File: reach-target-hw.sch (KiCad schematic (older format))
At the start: 53 parts, among them J101 CONN_01X02, J102 CONN_01X02, J103 CONN_02X05, J104 MODULE_HEADER, J105 MODULE_HEADER, J106 MODULE_HEADER, P101 CONN_01X05, P102 CONN_01X05, P103 CONN_01X02, P104 CONN_01X02, P105 CONN_01X05, P106 CONN_01X05, SW101 SW_PUSH, U1 nRF51822-QF, U101 CAT24C02YI-GT3A, U102 NCP103AMX330, X1 CX2520DB16000D0GEJCC, X2 SC32S-12.5PF20PPM

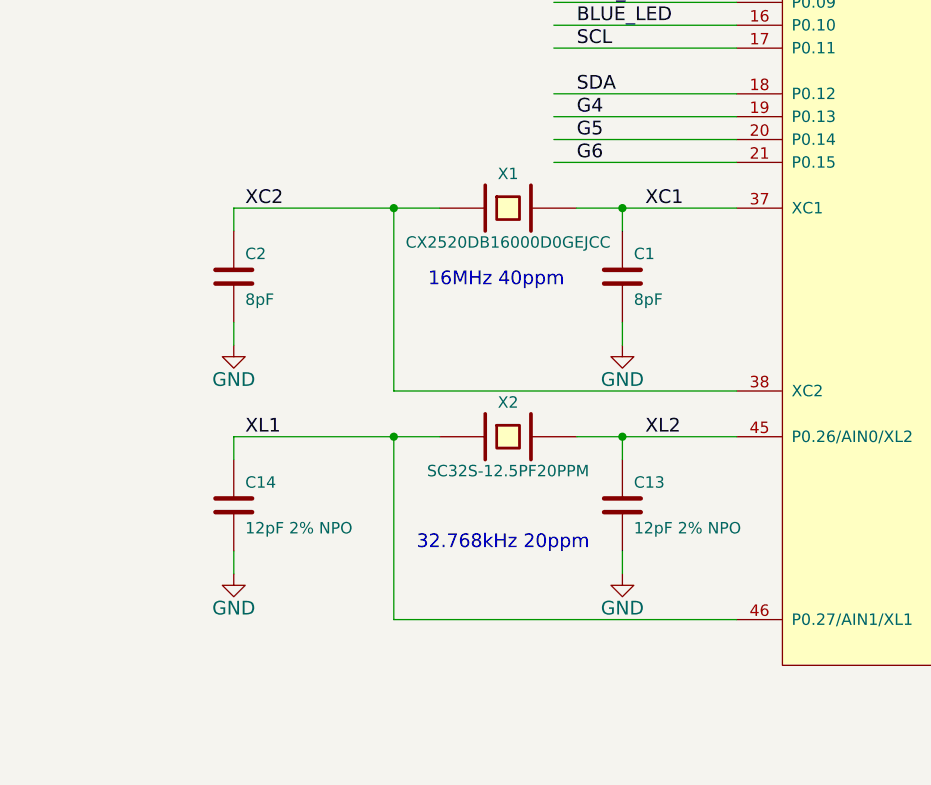
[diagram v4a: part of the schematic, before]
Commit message: ignore the last message... tweaked battery monitor, found real crystals
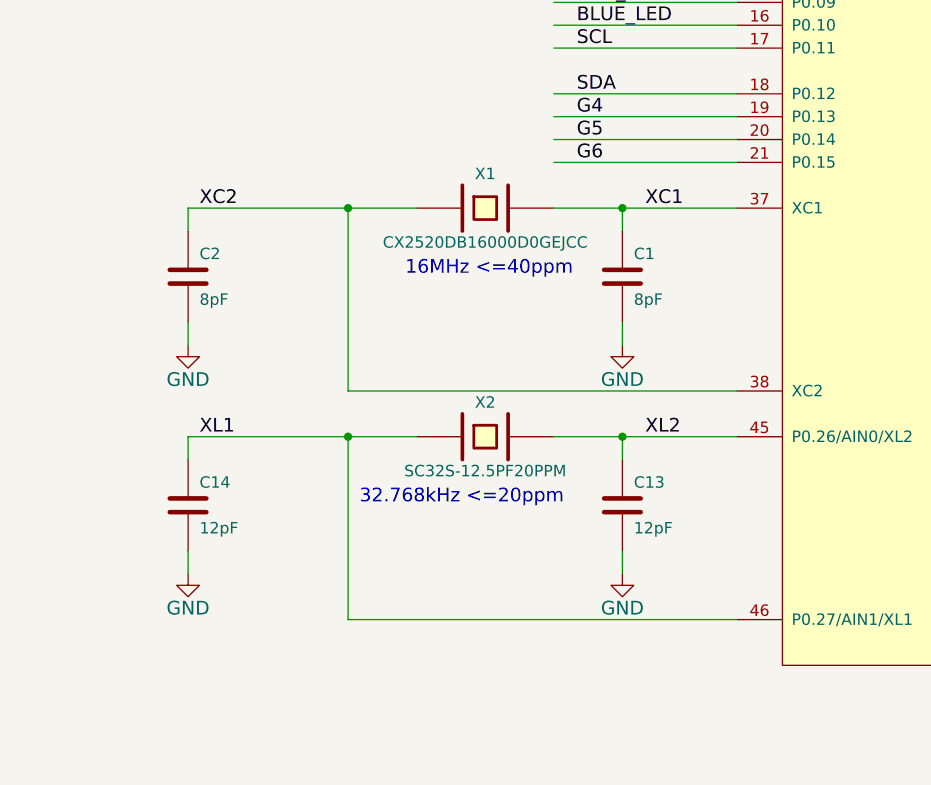
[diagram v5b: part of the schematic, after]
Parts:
- C13, C14: value 12pF 2% NPO -> 12pF
- X1: footprint (none) -> !Parts:CX2520DB
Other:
- note added: "16MHz <=40ppm"
- note added: "32.768kHz <=20ppm"
- note removed: "16MHz 40ppm"
- note removed: "32.768kHz 20ppm"
- moved on the sheet: C14, C2, X1, X2
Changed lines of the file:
@@
 L CRYSTAL X1
 U 1 1 54D12781
-P 6500 5200
-F 0 "X1" H 6500 5350 50  0000 C CNN
-F 1 "CX2520DB16000D0GEJCC" H 6500 5050 50  0000 C CNN
-F 2 "" H 6500 5200 60  0001 C CNN
-F 3 "" H 6500 5200 60  0000 C CNN
-	1    6500 5200
+P 6400 5200
+F 0 "X1" H 6400 5350 50  0000 C CNN
+F 1 "CX2520DB16000D0GEJCC" H 6400 5050 50  0000 C CNN
+F 2 "!Parts:CX2520DB" H 6400 5200 60  0001 C CNN
+F 3 "http://www.kyocera-crystal.jp/eng/wp-content/uploads/2014/09/cx2520db_e.pdf" H 6400 5200 60  0001 C CNN
+	1    6400 5200
 	1    0    0    -1
 $EndComp
@@
 L C C2
 U 1 1 54D14813
-P 5300 5500
-F 0 "C2" H 5350 5600 50  0000 L CNN
-F 1 "8pF" H 5350 5400 50  0000 L CNN
-F 2 "!Parts:SMD-0402" H 5338 5350 30  0001 C CNN
-F 3 "" H 5300 5500 60  0000 C CNN
-	1    5300 5500
+P 5100 5500
+F 0 "C2" H 5150 5600 50  0000 L CNN
+F 1 "8pF" H 5150 5400 50  0000 L CNN
+F 2 "!Parts:SMD-0402" H 5138 5350 30  0001 C CNN
+F 3 "" H 5100 5500 60  0000 C CNN
+	1    5100 5500
 	1    0    0    -1
 $EndComp
@@
 L GND #PWR06
 U 1 1 54D14CAE
-P 5300 5800
-F 0 "#PWR06" H 5300 5550 60  0001 C CNN
-F 1 "GND" H 5300 5650 60  0000 C CNN
-F 2 "" H 5300 5800 60  0000 C CNN
-F 3 "" H 5300 5800 60  0000 C CNN
-	1    5300 5800
+P 5100 5800
+F 0 "#PWR06" H 5100 5550 60  0001 C CNN
+F 1 "GND" H 5100 5650 60  0000 C CNN
+F 2 "" H 5100 5800 60  0000 C CNN
+F 3 "" H 5100 5800 60  0000 C CNN
+	1    5100 5800
 	1    0    0    -1
 $EndComp
@@
 L CRYSTAL X2
 U 1 1 54D14E4C
-P 6500 6200
-F 0 "X2" H 6500 6350 50  0000 C CNN
-F 1 "SC32S-12.5PF20PPM" H 6500 6050 50  0000 C CNN
-F 2 "!Parts:FC-135" H 6500 6200 60  0001 C CNN
-F 3 "http://www.sii.co.jp/en/quartz/files/2013/03/file_PRODUCT_MASTER_50812_GRAPHIC03.pdf" H 6500 6200 60  0001 C CNN
-	1    6500 6200
+P 6400 6200
+F 0 "X2" H 6400 6350 50  0000 C CNN
+F 1 "SC32S-12.5PF20PPM" H 6400 6050 50  0000 C CNN
+F 2 "!Parts:FC-135" H 6400 6200 60  0001 C CNN
+F 3 "http://www.sii.co.jp/en/quartz/files/2013/03/file_PRODUCT_MASTER_50812_GRAPHIC03.pdf" H 6400 6200 60  0001 C CNN
+	1    6400 6200
 	1    0    0    -1
 $EndComp
@@
 P 7000 6500
 F 0 "C13" H 7050 6600 50  0000 L CNN
-F 1 "12pF 2% NPO" H 7050 6400 50  0000 L CNN
+F 1 "12pF" H 7050 6400 50  0000 L CNN
 F 2 "!Parts:SMD-0402" H 7038 6350 30  0001 C CNN
 F 3 "" H 7000 6500 60  0000 C CNN
@@
 L C C14
 U 1 1 54D14E66
-P 5300 6500
-F 0 "C14" H 5350 6600 50  0000 L CNN
-F 1 "12pF 2% NPO" H 5350 6400 50  0000 L CNN
-F 2 "!Parts:SMD-0402" H 5338 6350 30  0001 C CNN
-F 3 "" H 5300 6500 60  0000 C CNN
-	1    5300 6500
+P 5100 6500
+F 0 "C14" H 5150 6600 50  0000 L CNN
+F 1 "12pF" H 5150 6400 50  0000 L CNN
+F 2 "!Parts:SMD-0402" H 5138 6350 30  0001 C CNN
+F 3 "" H 5100 6500 60  0000 C CNN
+	1    5100 6500
 	1    0    0    -1
 $EndComp
@@
 L GND #PWR08
 U 1 1 54D14E6F
-P 5300 6800
-F 0 "#PWR08" H 5300 6550 60  0001 C CNN
-F 1 "GND" H 5300 6650 60  0000 C CNN
-F 2 "" H 5300 6800 60  0000 C CNN
-F 3 "" H 5300 6800 60  0000 C CNN
-	1    5300 6800
+P 5100 6800
+F 0 "#PWR08" H 5100 6550 60  0001 C CNN
+F 1 "GND" H 5100 6650 60  0000 C CNN
+F 2 "" H 5100 6800 60  0000 C CNN
+F 3 "" H 5100 6800 60  0000 C CNN
+	1    5100 6800
 	1    0    0    -1
 $EndComp
@@
 Text Label 7100 5200 0    60   ~ 0
 XC1
-Text Label 5350 5200 0    60   ~ 0
+Text Label 5150 5200 0    60   ~ 0
 XC2
-Text Label 5350 6200 0    60   ~ 0
+Text Label 5150 6200 0    60   ~ 0
 XL1
 Text Label 7100 6200 0    60   ~ 0
@@
 	9900 2900 10100 2900
 Wire Wire Line
-	5300 6800 5300 6700
-Wire Wire Line
-	6000 7000 7500 7000
-Connection ~ 6000 6200
-Wire Wire Line
-	5300 6200 5300 6300
-Wire Wire Line
-	5300 6200 6000 6200
-Wire Wire Line
-	6000 6200 6200 6200
-Wire Wire Line
-	6000 7000 6000 6200
+	5100 6800 5100 6700
+Wire Wire Line
+	5800 7000 7500 7000
+Connection ~ 5800 6200
+Wire Wire Line
+	5100 6200 5100 6300
+Wire Wire Line
+	5100 6200 5800 6200
+Wire Wire Line
+	5800 6200 6100 6200
+Wire Wire Line
+	5800 7000 5800 6200
 Connection ~ 7000 6200
 Wire Wire Line
@@
 	7000 6800 7000 6700
 Wire Wire Line
-	6800 6200 7000 6200
+	6700 6200 7000 6200
 Wire Wire Line
 	7000 6200 7500 6200
 Wire Wire Line
-	5300 5800 5300 5700
-Wire Wire Line
-	6000 6000 7500 6000
-Connection ~ 6000 5200
-Wire Wire Line
-	5300 5200 5300 5300
-Wire Wire Line
-	5300 5200 6000 5200
-Wire Wire Line
-	6000 5200 6200 5200
-Wire Wire Line
-	6000 6000 6000 5200
+	5100 5800 5100 5700
+Wire Wire Line
+	5800 6000 7500 6000
+Connection ~ 5800 5200
+Wire Wire Line
+	5100 5200 5100 5300
+Wire Wire Line
+	5100 5200 5800 5200
+Wire Wire Line
+	5800 5200 6100 5200
+Wire Wire Line
+	5800 6000 5800 5200
 Connection ~ 7000 5200
 Wire Wire Line
@@
 	7000 5800 7000 5700
 Wire Wire Line
-	6800 5200 7000 5200
+	6700 5200 7000 5200
 Wire Wire Line
 	7000 5200 7500 5200
@@
 Text Label 2350 2800 0    60   ~ 0
 BATT_GAUGE
-Text Notes 6100 6700 0    60   ~ 0
-32.768kHz 20ppm
-Text Notes 6150 5550 0    60   ~ 0
-16MHz 40ppm
+Text Notes 5850 6500 0    60   ~ 0
+32.768kHz <=20ppm
+Text Notes 6050 5500 0    60   ~ 0
+16MHz <=40ppm
 $EndSCHEMATC

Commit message: "last" schematic changes
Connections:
- wire segments 255 -> 216
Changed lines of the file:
@@
 	2900 2800 2900 2900
 Wire Wire Line
-	2200 2800 2300 2800
-Wire Wire Line
-	2300 2800 2900 2800
-Wire Wire Line
-	2900 2800 3100 2800
+	2200 2800 3100 2800
 Wire Wire Line
 	2600 2300 2600 2200
@@
 	2600 1700 2600 1800
 Wire Wire Line
-	1500 1700 1700 1700
-Wire Wire Line
-	1700 1700 2200 1700
-Wire Wire Line
-	2200 1700 2600 1700
-Wire Wire Line
-	2600 1700 3000 1700
+	1500 1700 3000 1700
 Wire Wire Line
 	3000 2400 3800 2400
@@
 	5300 2800 5200 2800
 Wire Wire Line
-	5300 2700 5300 2800
-Wire Wire Line
-	5300 2800 5300 3000
+	5300 2700 5300 3000
 Wire Wire Line
 	5200 2700 5300 2700
 Wire Wire Line
-	5200 2400 5600 2400
-Wire Wire Line
-	5600 2400 5700 2400
+	5200 2400 5700 2400
 Wire Wire Line
 	5700 2400 5700 2200
@@
 	12000 5100 12000 5200
 Wire Wire Line
-	11800 5100 12000 5100
-Wire Wire Line
-	12000 5100 12400 5100
+	11800 5100 12400 5100
 Connection ~ 11000 5100
 Wire Wire Line
@@
 	11000 5100 11000 5200
 Wire Wire Line
-	10800 5100 11000 5100
-Wire Wire Line
-	11000 5100 11200 5100
+	10800 5100 11200 5100
 Connection ~ 10200 5100
 Connection ~ 10100 6900
@@
 	10200 5100 10200 5200
 Wire Wire Line
-	9900 5100 10200 5100
-Wire Wire Line
-	10200 5100 10400 5100
-Wire Wire Line
-	10100 6800 10100 6900
-Wire Wire Line
-	10100 6900 10100 7000
+	9900 5100 10400 5100
+Wire Wire Line
+	10100 6800 10100 7000
 Wire Wire Line
 	9900 6900 10100 6900
@@
 	10200 6000 10200 5800
 Wire Wire Line
-	9900 6000 10100 6000
-Wire Wire Line
-	10100 6000 10200 6000
+	9900 6000 10200 6000
 Connection ~ 8800 2300
 Wire Wire Line
@@
 	8800 2300 8700 2300
 Wire Wire Line
-	8800 1400 8800 2300
-Wire Wire Line
-	8800 2300 8800 2400
+	8800 1400 8800 2400
 Wire Wire Line
 	11100 1400 11100 1600
@@
 	11800 2900 11800 3000
 Wire Wire Line
-	11700 2900 11800 2900
-Wire Wire Line
-	11800 2900 12600 2900
+	11700 2900 12600 2900
 Wire Wire Line
 	10700 2900 11100 2900
@@
 	5100 6200 5100 6300
 Wire Wire Line
-	5100 6200 5800 6200
-Wire Wire Line
-	5800 6200 6100 6200
+	5100 6200 6100 6200
 Wire Wire Line
 	5800 7000 5800 6200
@@
 	7000 6800 7000 6700
 Wire Wire Line
-	6700 6200 7000 6200
-Wire Wire Line
-	7000 6200 7500 6200
+	6700 6200 7500 6200
 Wire Wire Line
 	5100 5800 5100 5700
@@
 	5100 5200 5100 5300
 Wire Wire Line
-	5100 5200 5800 5200
-Wire Wire Line
-	5800 5200 6100 5200
+	5100 5200 6100 5200
 Wire Wire Line
 	5800 6000 5800 5200
@@
 	7000 5800 7000 5700
 Wire Wire Line
-	6700 5200 7000 5200
-Wire Wire Line
-	7000 5200 7500 5200
+	6700 5200 7500 5200
 Connection ~ 8400 2300
 Connection ~ 8500 2300
@@
 	8400 2300 8500 2300
 Wire Wire Line
-	8500 1450 8500 2300
-Wire Wire Line
-	8500 2300 8500 2400
+	8500 1450 8500 2400
 Wire Wire Line
 	6800 1450 8500 1450
 Wire Wire Line
-	6800 1150 6800 1450
-Wire Wire Line
-	6800 1450 6800 1600
+	6800 1150 6800 1600
 Wire Wire Line
 	6800 2100 6800 2000
@@
 	8400 1500 7600 1500
 Wire Wire Line
-	8400 1500 8400 2300
-Wire Wire Line
-	8400 2300 8400 2400
+	8400 1500 8400 2400
 Wire Wire Line
 	7600 2100 7600 2000
@@
 Connection ~ 8500 7500
 Wire Wire Line
-	8500 7500 8600 7500
-Wire Wire Line
-	8600 7500 8700 7500
-Wire Wire Line
-	8700 7500 8900 7500
+	8500 7500 8900 7500
 Wire Wire Line
 	8600 7400 8600 7500
 Wire Wire Line
-	8500 7400 8500 7500
-Wire Wire Line
-	8500 7500 8500 7600
+	8500 7400 8500 7600
 Wire Wire Line
 	4100 5200 3200 5200
@@
 	1700 7200 1700 7000
 Wire Wire Line
-	2400 7200 2600 7200
-Wire Wire Line
-	2600 7200 3000 7200
-Wire Wire Line
-	3000 7200 3700 7200
+	2400 7200 3700 7200
 Wire Wire Line
 	2600 7300 2600 7200
@@
 	7900 9000 9800 9000
 Wire Wire Line
-	7200 9100 7200 9200
-Wire Wire Line
-	7200 9200 7200 9500
+	7200 9100 7200 9500
 Wire Wire Line
 	7200 9200 7400 9200
@@
 	7400 9300 6700 9300
 Wire Wire Line
-	9800 8900 9800 9000
-Wire Wire Line
-	9800 9000 9800 9100
+	9800 8900 9800 9100
 Connection ~ 9800 9000
 Wire Wire Line
@@
 	1500 1800 1600 1800
 Wire Wire Line
-	1600 1800 1600 2400
-Wire Wire Line
-	1600 2400 1600 2600
+	1600 1800 1600 2600
 Wire Wire Line
 	1500 2400 1600 2400
@@
 	15100 6100 14700 6100
 Wire Wire Line
-	14700 6100 14700 6400
-Wire Wire Line
-	14700 6400 14700 7000
-Wire Wire Line
-	14700 7000 14700 7600
-Wire Wire Line
-	14700 7600 14700 8200
-Wire Wire Line
-	14700 8200 14700 8800
-Wire Wire Line
-	14700 8800 14700 9000
+	14700 6100 14700 9000
 Wire Wire Line
 	14800 8800 14700 8800
@@
 	15100 6200 14600 6200
 Wire Wire Line
-	14600 6000 14600 6200
-Wire Wire Line
-	14600 6200 14600 6500
-Wire Wire Line
-	14600 6500 14600 7100
-Wire Wire Line
-	14600 7100 14600 7700
-Wire Wire Line
-	14600 7700 14600 8300
-Wire Wire Line
-	14600 8300 14600 8900
+	14600 6000 14600 8900
 Wire Wire Line
 	14600 6500 14800 6500

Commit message: done goofed and did inconsistent refdes numbering. reset.
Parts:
- AE1: renamed from AE101; footprint (none) -> !Parts:ANTENNA-SMT-2.45GHz
- renumbered C101 to C1, C7 to C10, C10 to C11, C3 to C12, C8 to C13, C5 to C14, C4 to C15, C9 to C16, C12 to C17, C6 to C18, C102 to C2, C103 to C3, C2 to C4, C14 to C5, C104 to C6, C11 to C7, C1 to C8, C13 to C9, D101 to D1, D102 to D2, J101 to J1, J102 to J2, J103 to J3, J104 to J4, J105 to J5, J106 to J6, L2 to L1, L1 to L2, L4 to L3, L5 to L4, L3 to L5, P101 to P1, P102 to P2, P103 to P3, P104 to P4, P105 to P5, P106 to P6, R101 to R1, R102 to R2, R103 to R3, R104 to R4, R109 to R5, R105 to R6, R106 to R7, R107 to R8, R108 to R9, SW101 to SW1, U101 to U1, U102 to U2, U1 to U3

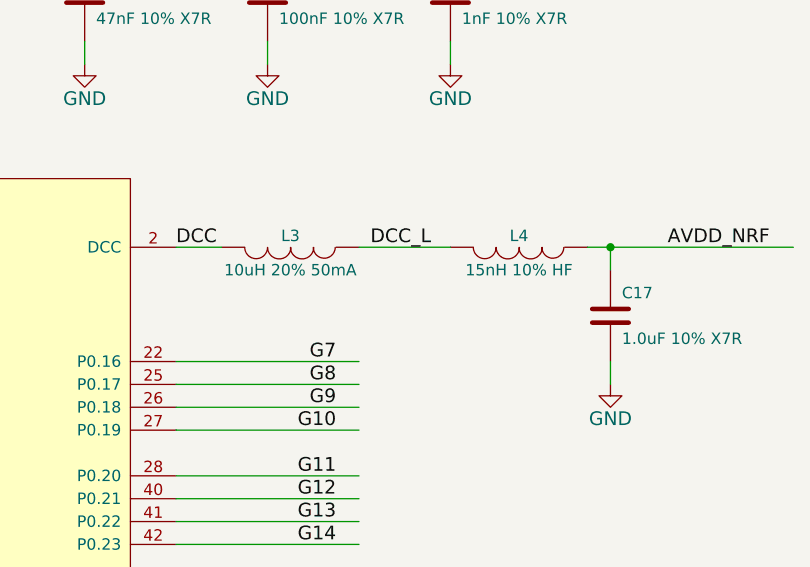
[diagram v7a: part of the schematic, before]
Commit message: dcdc inductors
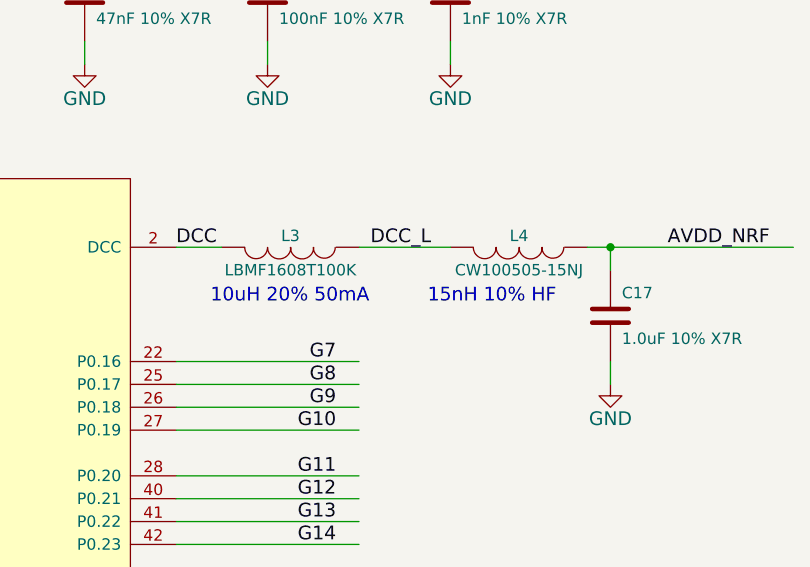
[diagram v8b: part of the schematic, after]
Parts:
- L3: value 10uH 20% 50mA -> LBMF1608T100K
- L4: value 15nH 10% HF -> CW100505-15NJ
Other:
- note added: "10uH 20% 50mA"
- note added: "15nH 10% HF"
